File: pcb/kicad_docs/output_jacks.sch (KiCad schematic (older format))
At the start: 8 parts, among them J1 PJ301M-12, J2 PJ301M-12, J3 PJ301M-12, J4 PJ301M-12

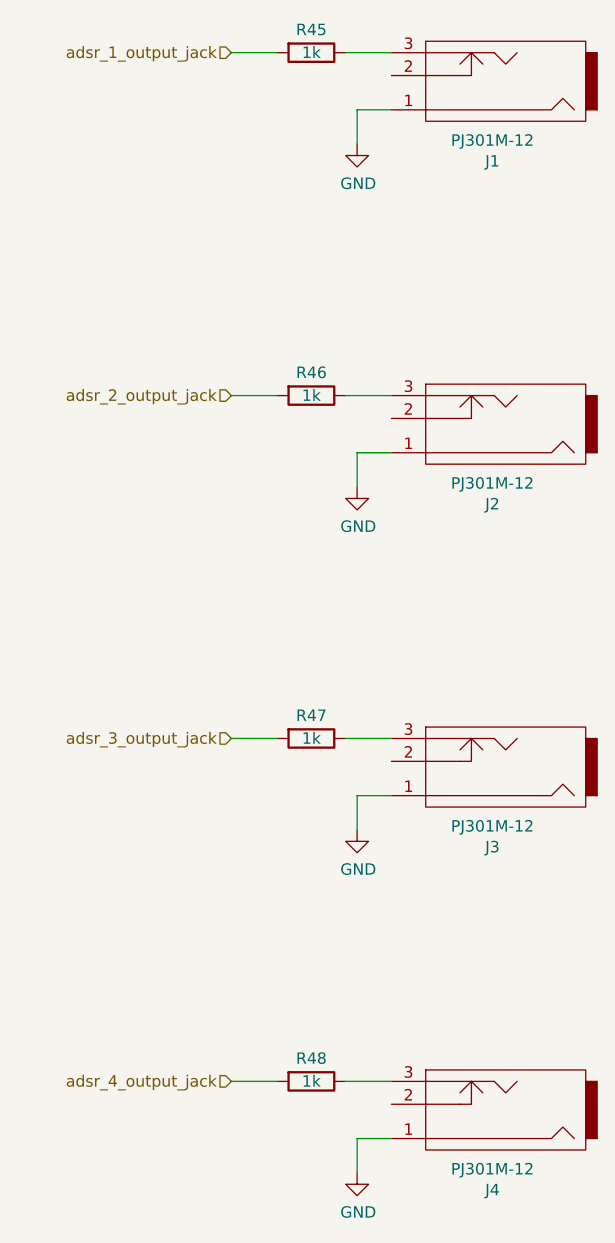
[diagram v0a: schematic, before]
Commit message: add title blocks, fix some erc violations
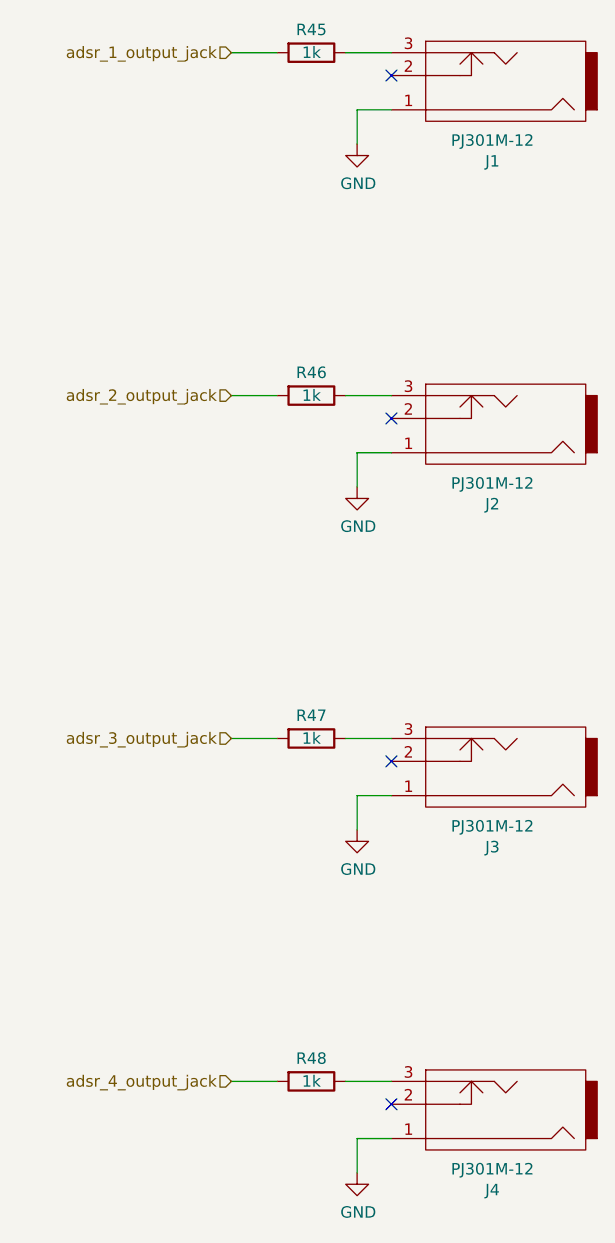
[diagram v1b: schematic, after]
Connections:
- no-connect marks 0 -> 4
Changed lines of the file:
@@
 $Descr A4 11693 8268
 encoding utf-8
-Sheet 5 10
-Title ""
-Date ""
-Rev ""
+Sheet 4 10
+Title "Quad ADSR"
+Date "2020-07-31"
+Rev "0"
 Comp ""
-Comment1 ""
-Comment2 ""
-Comment3 ""
+Comment1 "creativecommons.org/licenses/by/4.0/"
+Comment2 "License: CC by 4.0"
+Comment3 "Author: Jordan Aceto"
 Comment4 ""
 $EndDescr
@@
 Wire Wire Line
 	4400 6000 4600 6000
+NoConn ~ 5100 1600
+NoConn ~ 5100 3100
+NoConn ~ 5100 4600
+NoConn ~ 5100 6100
 $EndSCHEMATC
